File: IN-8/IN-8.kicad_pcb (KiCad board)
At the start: 2 copper layers, 60.9 x 72.2 mm, 97 parts, among them J1 USB_C_Receptacle_USB2.0, Q1 MMBTA92, Q10 MMBTA42, Q11 MMBTA42, Q12 MMBTA42, Q13 MMBTA42, Q14 MMBTA92, Q15 10N20L, Q2 MMBTA42, Q3 MMBTA42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

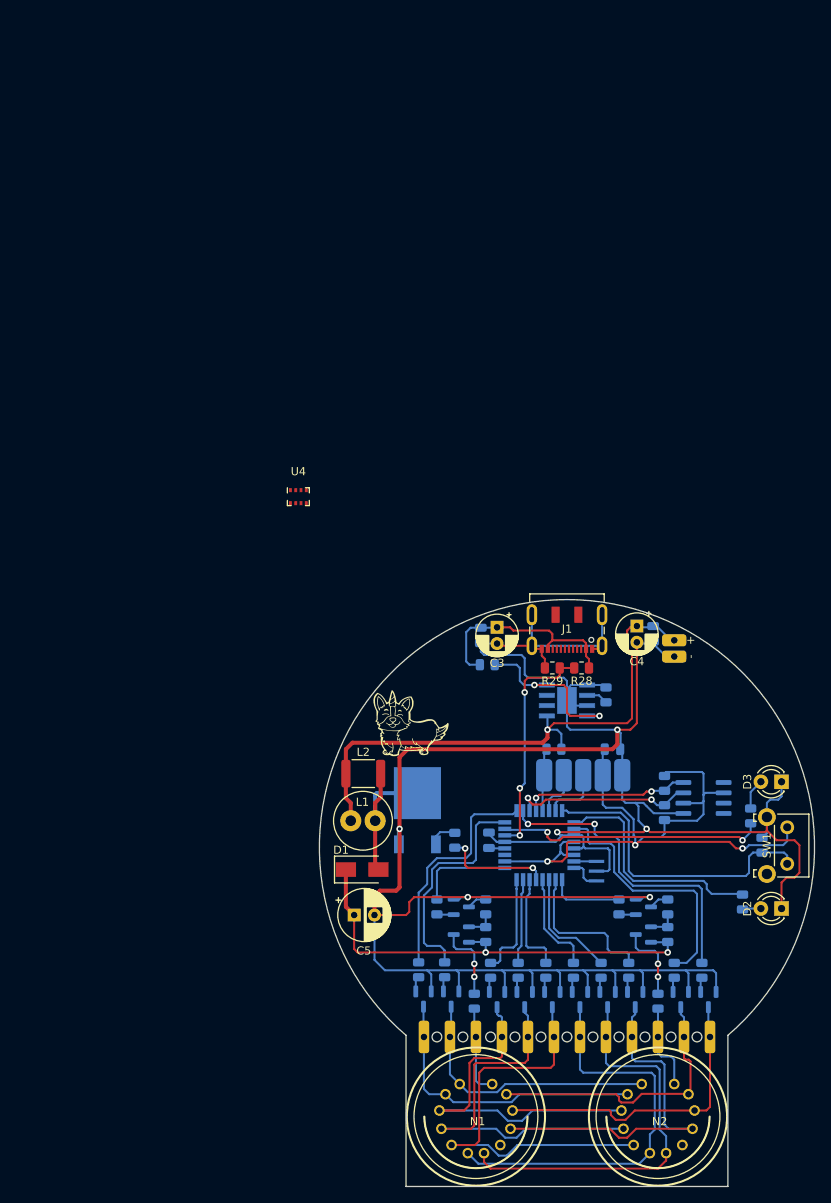
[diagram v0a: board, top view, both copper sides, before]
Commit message: KiCad project updaated, gitignore added
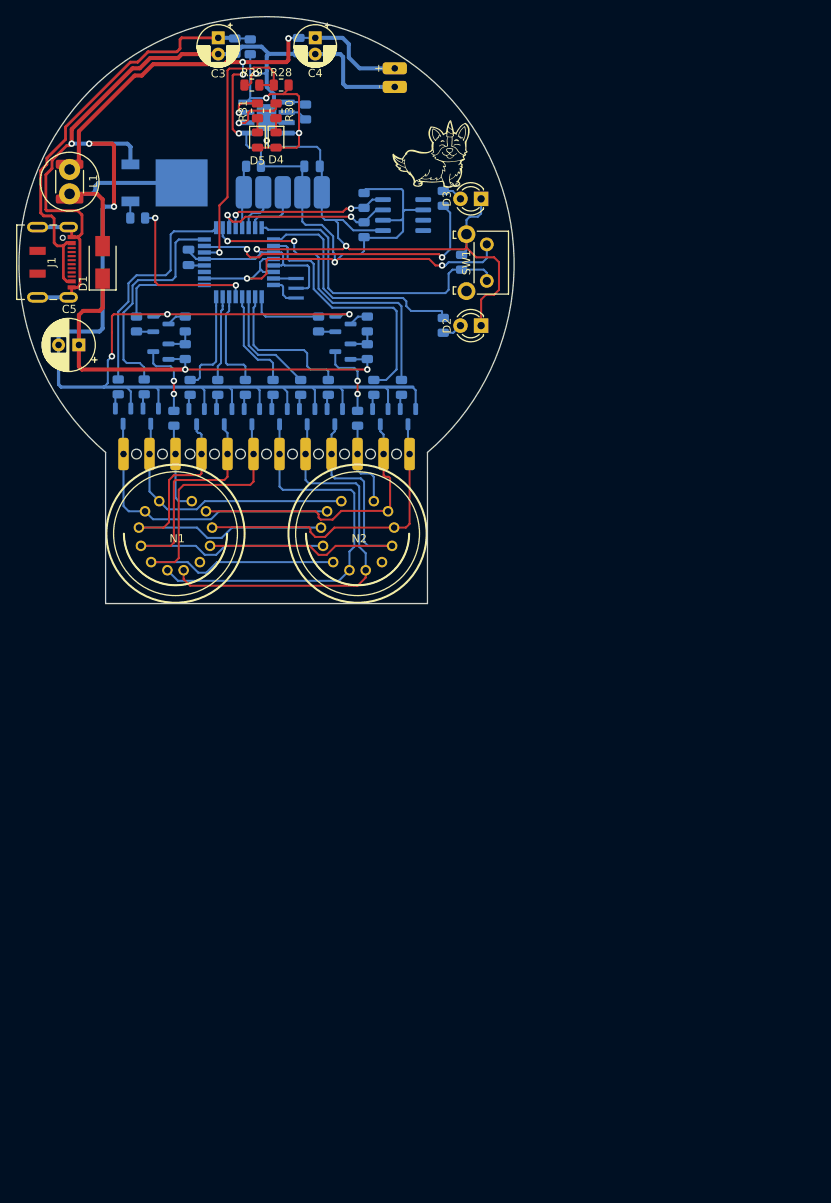
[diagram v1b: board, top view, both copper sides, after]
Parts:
- removed U4: BMP280, Package_LGA:Bosch_LGA-8_2x2.5mm_P0.65mm_ClockwisePinNumbering
- added D4: STB, LED_SMD:LED_0805_2012Metric, F.Cu at (161.0, 31.8)
- added D5: CHR, LED_SMD:LED_0805_2012Metric, F.Cu at (158.7, 31.8)
- added R30: 10k, Resistor_SMD:R_0805_2012Metric, F.Cu at (161.0, 28.3)
- added R31: 10k, Resistor_SMD:R_0805_2012Metric, F.Cu at (158.8, 28.3)
- R21: value 1k -> 10k
- moved G*** 98.2 mm to (148.4, 26.2)
- moved L1 87.3 mm to (135.6, 35.5), turned to -90 degrees
- moved R19 85.9 mm to (144.0, 41.4), turned to 180 degrees
- moved R24 84.9 mm to (181.6, 39.0)
- moved C7 84.5 mm to (163.8, 20.2)
- moved Q15 83.2 mm to (147.3, 37.1), turned to 0 degrees
- moved C4 82.5 mm to (165.9, 19.3)
- moved R20 81.4 mm to (157.9, 20.4), turned to 90 degrees
- moved L2 81.3 mm to (135.6, 37.0), turned to -90 degrees
- moved D1 81.2 mm to (139.7, 46.9), turned to 90 degrees
- moved D2 80.7 mm to (186.3, 54.7)
- moved Q12 80.7 mm to (146.9, 54.5)
- moved Q13 80.7 mm to (169.3, 54.5)
- moved R10 80.7 mm to (148.5, 66.1)
- moved R12 80.7 mm to (172.3, 54.5)
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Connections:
- net Net-(R22-Pad2) renamed Int
- net Net-(R23-Pad2) renamed M
- net Net-(R24-Pad2) renamed H
- net Net-(R26-Pad1) renamed SCL
- net Net-(R27-Pad1) renamed SDA
- C1 pad 1: Net-(C1-Pad1) -> GND
- C1 pad 2: GND -> Net-(C1-Pad2)
- C3 pad 1: Net-(C3-Pad1) -> VUSB
- C6 pad 1: Net-(C3-Pad1) -> VUSB
- J1 pad A4: Net-(C3-Pad1) -> VUSB
- J1 pad A9: Net-(C3-Pad1) -> VUSB
- J1 pad B4: Net-(C3-Pad1) -> VUSB
- J1 pad B9: Net-(C3-Pad1) -> VUSB
- R20 pad 1: Net-(R20-Pad1) -> 5V
- R20 pad 2: Net-(C3-Pad1) -> VUSB
- R28 pad 2: Net-(C3-Pad1) -> 5V
- SW1 pad : (no net) -> GND
- U1 pad 20: Net-(C1-Pad1) -> Net-(C1-Pad2)
- U2 pad 4: Net-(R20-Pad1) -> 5V
- U2 pad 6: unconnected-(U2-Pad6) -> STB
- U2 pad 7: unconnected-(U2-Pad7) -> CHR
- U2 pad 8: Net-(R20-Pad1) -> 5V
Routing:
- net VUSB: track 0.00 -> 52.3 mm
- net GND: track 344.4 -> 372.7 mm, vias 6 -> 10
- net 5V: track 0.00 -> 28.1 mm, vias 0 -> 2
- net Net-(C3-Pad1): track 26.2 -> 0.00 mm
- net Net-(R20-Pad1): track 22.1 -> 0.00 mm, vias 2 -> 0
- net PWM: track 13.5 -> 20.6 mm
- net UsbCon: track 28.2 -> 35.0 mm, vias 3 -> 1
- net STB: track 0.00 -> 6.46 mm, vias 0 -> 1
- net H: track 33.0 -> 37.6 mm
- net Net-(D1-Pad2): track 21.3 -> 25.7 mm
- net CHR: track 0.00 -> 3.29 mm, vias 0 -> 1
- net Net-(C1-Pad2): track 0.00 -> 2.17 mm
- net Net-(C1-Pad1): track 2.17 -> 0.00 mm
- net Net-(D5-Pad1): track 0.00 -> 1.74 mm
- net Net-(D4-Pad1): track 0.00 -> 1.74 mm
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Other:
- board text added: "15.10.22"
- board text removed: "08.09.22"
